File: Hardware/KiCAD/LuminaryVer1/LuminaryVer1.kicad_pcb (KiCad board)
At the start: 2 copper layers, 31 parts, among them J1 SPI_1_Connections, J10 ExtBattPwr, J2 SPI_2_Connections, J3 CAN_Connections, J4 ADC_Connections, J5 I2C_1_Connections, J6 I2C_2_Connections, J7 RS232_1_Connections, J8 RS232_2_Connections, J9 RS232_3_Connections, U1 74HC14, U2 STM32L432KBUx

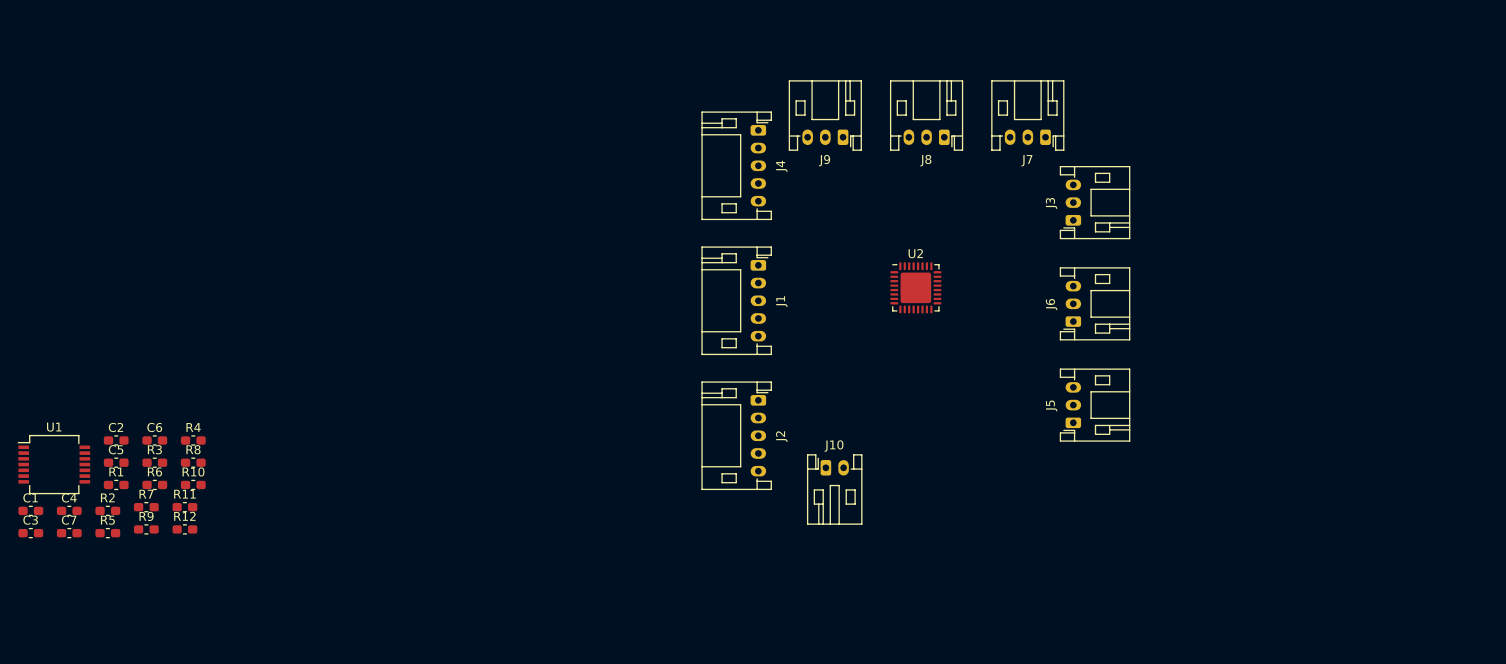
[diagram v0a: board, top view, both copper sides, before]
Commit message: Added PMIC and charging circuitry. Minor refresh of existing components. Added KiCAD component lib.
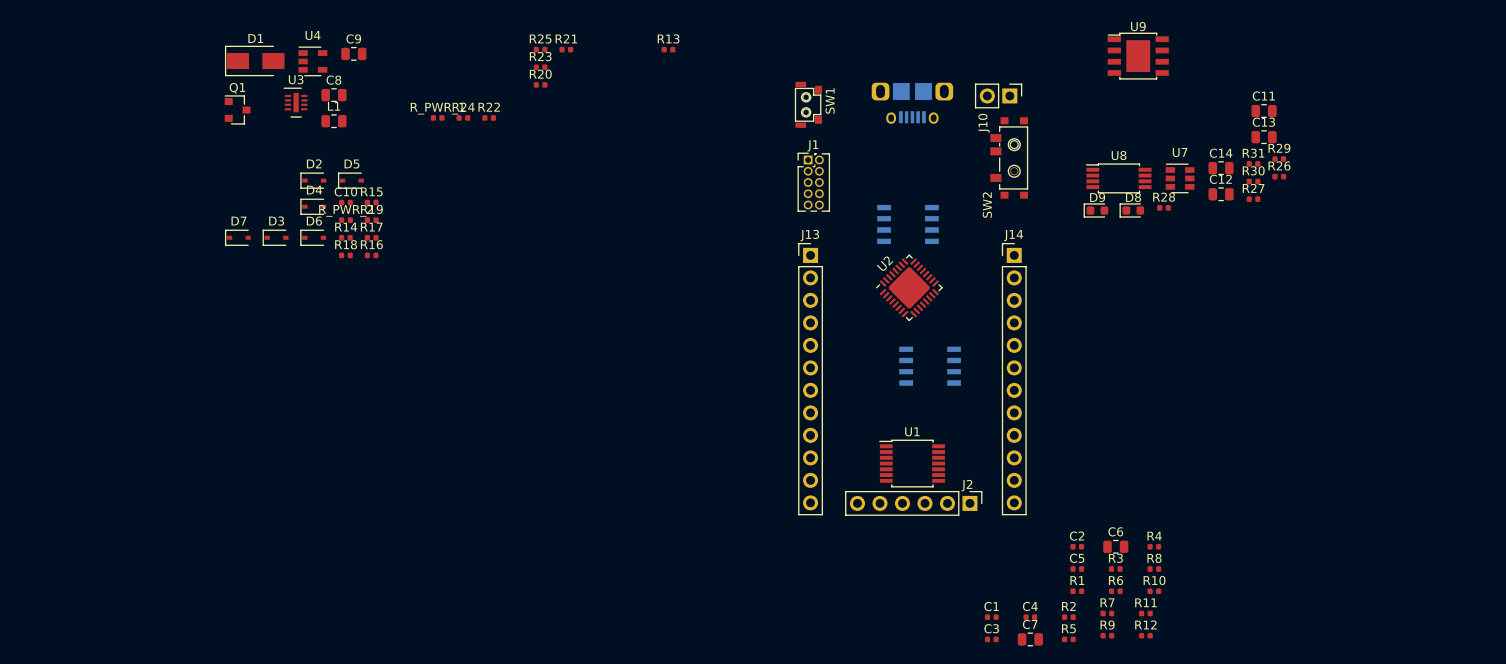
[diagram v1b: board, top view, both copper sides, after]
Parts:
- removed J3: CAN_Connections, Connector_JST:JST_PH_S3B-PH-K_1x03_P2.00mm_Horizontal
- removed J4: ADC_Connections, Connector_JST:JST_PH_S5B-PH-K_1x05_P2.00mm_Horizontal
- removed J5: I2C_1_Connections, Connector_JST:JST_PH_S3B-PH-K_1x03_P2.00mm_Horizontal
- removed J6: I2C_2_Connections, Connector_JST:JST_PH_S3B-PH-K_1x03_P2.00mm_Horizontal
- removed J7: RS232_1_Connections, Connector_JST:JST_PH_S3B-PH-K_1x03_P2.00mm_Horizontal
- removed J8: RS232_2_Connections, Connector_JST:JST_PH_S3B-PH-K_1x03_P2.00mm_Horizontal
- removed J9: RS232_3_Connections, Connector_JST:JST_PH_S3B-PH-K_1x03_P2.00mm_Horizontal
- added C10: 100nF, Capacitor_SMD:C_0402_1005Metric, F.Cu at (160.4, 64.0)
- added C11: 100nF, Capacitor_SMD:C_0805_2012Metric, F.Cu at (264.1, 53.7)
- added C12: 1uF, Capacitor_SMD:C_0805_2012Metric, F.Cu at (259.2, 63.1)
- added C13: 100nF, Capacitor_SMD:C_0805_2012Metric, F.Cu at (264.1, 56.6)
- added C14: 10uF, Capacitor_SMD:C_0805_2012Metric, F.Cu at (259.2, 60.1)
- added C8: 1uF, Capacitor_SMD:C_0805_2012Metric, F.Cu at (159.1, 51.9)
- added C9: 1uF, Capacitor_SMD:C_0805_2012Metric, F.Cu at (161.3, 47.2)
- added D1: SS16HE, Diode_SMD:D_SMA, F.Cu at (150.3, 48.0)
- added D2: 3v3Zener, Diode_SMD:D_SOD-323, F.Cu at (156.9, 61.6)
- added D3: 3v3Zener, Diode_SMD:D_SOD-323, F.Cu at (152.6, 68.0)
- added D4: 3v3Zener, Diode_SMD:D_SOD-323, F.Cu at (156.9, 64.5)
- added D5: 3v3Zener, Diode_SMD:D_SOD-323, F.Cu at (161.1, 61.6)
- added D6: 3v3Zener, Diode_SMD:D_SOD-323, F.Cu at (156.9, 68.0)
- added D7: 3v3Zener, Diode_SMD:D_SOD-323, F.Cu at (148.4, 68.0)
- added D8: RLED, Diode_SMD:D_0603_1608Metric, F.Cu at (249.3, 64.9)
- added D9: BLED, Diode_SMD:D_0603_1608Metric, F.Cu at (245.3, 64.9)
- added J12: USB_B_Micro, USB:Amphenol-MicroB, B.Cu at (224.4, 51.5)
- added J13: CN1, Connector_PinHeader_2.54mm:PinHeader_1x12_P2.54mm_Vertical, F.Cu at (212.9, 70.0)
- added J14: CN2, Connector_PinHeader_2.54mm:PinHeader_1x12_P2.54mm_Vertical, F.Cu at (235.9, 70.0)
- added L1: 4.3uH, Inductor_SMD:L_0805_2012Metric, F.Cu at (159.1, 54.9)
- added Q1: 2N3904, Package_TO_SOT_SMD:SOT-23, F.Cu at (148.2, 53.6)
- added R13: 0, Resistor_SMD:R_0402_1005Metric, F.Cu at (196.9, 46.8)
- added R14: 1.8k, Resistor_SMD:R_0402_1005Metric, F.Cu at (160.4, 68.0)
- added R15: 1.8k, Resistor_SMD:R_0402_1005Metric, F.Cu at (163.4, 64.0)
- added R16: 1.8k, Resistor_SMD:R_0402_1005Metric, F.Cu at (163.3, 70.0)
- added R17: 1.8k, Resistor_SMD:R_0402_1005Metric, F.Cu at (163.3, 68.0)
- added R18: 1.8k, Resistor_SMD:R_0402_1005Metric, F.Cu at (160.4, 70.0)
- added R19: 1.8k, Resistor_SMD:R_0402_1005Metric, F.Cu at (163.4, 66.0)
- added R20: 50k, Resistor_SMD:R_0402_1005Metric, F.Cu at (182.4, 50.8)
- added R21: 50k, Resistor_SMD:R_0402_1005Metric, F.Cu at (185.3, 46.8)
- added R22: 50k, Resistor_SMD:R_0402_1005Metric, F.Cu at (176.6, 54.5)
- added R23: 50k, Resistor_SMD:R_0402_1005Metric, F.Cu at (182.4, 48.8)
- added R24: 50k, Resistor_SMD:R_0402_1005Metric, F.Cu at (173.7, 54.5)
- added R25: 50k, Resistor_SMD:R_0402_1005Metric, F.Cu at (182.4, 46.8)
- added R26: 1k, Resistor_SMD:R_0402_1005Metric, F.Cu at (265.8, 61.1)
- added R27: 1k, Resistor_SMD:R_0402_1005Metric, F.Cu at (262.9, 63.6)
- added R28: 1k, Resistor_SMD:R_0402_1005Metric, F.Cu at (252.8, 64.6)
- added R29: 10k, Resistor_SMD:R_0402_1005Metric, F.Cu at (265.8, 59.1)
- added R30: 100, Resistor_SMD:R_0402_1005Metric, F.Cu at (262.9, 61.7)
- added R31: 50k, Resistor_SMD:R_0402_1005Metric, F.Cu at (262.9, 59.7)
- added R_PWR_1: 0, Resistor_SMD:R_0402_1005Metric, F.Cu at (170.8, 54.5)
- added R_PWR_2: 0, Resistor_SMD:R_0402_1005Metric, F.Cu at (160.4, 66.0)
- added SW1: SW_Push, button:LCSC_C255808_HYP_2x4x3.5mm_RightAngle, F.Cu at (212.4, 53.0)
- added SW2: SW_BATT_DISCONNECT, toggle:LCSC_C136659_HRO_SPDT_6.7x2.6mm_ToggleSwitch, F.Cu at (235.9, 59.0)
- added U3: DIO6605, Package_DFN_QFN:DFN-8-1EP_2x3mm_P0.5mm_EP0.61x2.2mm, F.Cu at (154.8, 52.8)
- added U4: AP2112K-3.3, Package_TO_SOT_SMD:SOT-23-5, F.Cu at (156.7, 48.1)
- added U5: SN65HVD232, Package_SO:SOIC-8_3.9x4.9mm_P1.27mm, B.Cu at (226.4, 82.5)
- added U6: AT25SF081-SSHD-X, Package_SO:SOIC-8_3.9x4.9mm_P1.27mm, B.Cu at (223.9, 66.5)
- added U7: DW01, Package_TO_SOT_SMD:SOT-23-6, F.Cu at (254.6, 61.3)
- added U8: FS8205A, Package_SO:TSSOP-8_4.4x3mm_P0.65mm, F.Cu at (247.7, 61.3)
- added U9: TP4056, PMIC:TP4056_SOP-8-PP, F.Cu at (249.9, 47.5)
- C1, C2, C3, C4, C5: footprint Capacitor_SMD:C_0603_1608Metric_Pad1.05x0.95mm_HandSolder -> Capacitor_SMD:C_0402_1005Metric
- C6, C7: value 100nF -> 10uF; footprint Capacitor_SMD:C_0603_1608Metric_Pad1.05x0.95mm_HandSolder -> Capacitor_SMD:C_0805_2012Metric
- J1: value SPI_1_Connections -> JTAG; footprint Connector_JST:JST_PH_S5B-PH-K_1x05_P2.00mm_Horizontal -> Connector_PinHeader_1.27mm:PinHeader_2x05_P1.27mm_Vertical
- J10: footprint Connector_JST:JST_PH_S2B-PH-K_1x02_P2.00mm_Horizontal -> Connector_PinHeader_2.54mm:PinHeader_1x02_P2.54mm_Vertical
- J2: value SPI_2_Connections -> GPIOInput; footprint Connector_JST:JST_PH_S5B-PH-K_1x05_P2.00mm_Horizontal -> Connector_PinHeader_2.54mm:PinHeader_1x06_P2.54mm_Vertical
- R1, R10, R2, R4, R5, R6, R7: value 10k -> 50k; footprint Resistor_SMD:R_0603_1608Metric_Pad1.05x0.95mm_HandSolder -> Resistor_SMD:R_0402_1005Metric
- R11, R3, R9: footprint Resistor_SMD:R_0603_1608Metric_Pad1.05x0.95mm_HandSolder -> Resistor_SMD:R_0402_1005Metric
- R12: value 10k -> 120; footprint Resistor_SMD:R_0603_1608Metric_Pad1.05x0.95mm_HandSolder -> Resistor_SMD:R_0402_1005Metric
- R8: value 10k -> 100; footprint Resistor_SMD:R_0603_1608Metric_Pad1.05x0.95mm_HandSolder -> Resistor_SMD:R_0402_1005Metric
- U1: footprint Package_SO:SSOP-14_5.3x6.2mm_P0.65mm -> Package_SO:TSSOP-14_4.4x5mm_P0.65mm
- moved C1 109.2 mm to (233.4, 110.8)
- moved C2 109.2 mm to (243.0, 102.9)
- moved C3 109.2 mm to (233.4, 113.4)
- moved C4 109.2 mm to (237.7, 110.8)
- moved C5 109.2 mm to (243.0, 105.4)
- moved C6 109.2 mm to (247.4, 102.9)
- moved C7 109.2 mm to (237.7, 113.4)
- moved R1 109.2 mm to (243.0, 107.9)
- moved R10 109.2 mm to (251.7, 107.9)
- moved R11 109.2 mm to (250.8, 110.4)
- moved R12 109.2 mm to (250.8, 112.9)
- moved R2 109.2 mm to (242.1, 110.8)
- moved R3 109.2 mm to (247.4, 105.4)
- moved R4 109.2 mm to (251.7, 102.9)
- moved R5 109.2 mm to (242.1, 113.4)
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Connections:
- net Net-(U2-Pad10) renamed /Processor/ADC_2
- net Net-(U2-Pad29) renamed /Output Connectors/I2C_1_SCL
- net Net-(U2-Pad6) renamed /Processor/ADC_0
- net Net-(U2-Pad9) renamed /Processor/ADC_1
- C1 pad 1: Net-(C1-Pad1) -> GND
- C1 pad 2: GND -> /Input Connectors/nRESET
- C2 pad 1: Net-(C2-Pad1) -> GND
- C2 pad 2: GND -> Net-(C2-Pad2)
- C3 pad 1: Net-(C3-Pad1) -> +3V3
- C4 pad 1: Net-(C4-Pad1) -> GND
- C4 pad 2: GND -> +3V3
- C5 pad 1: Net-(C5-Pad1) -> GND
- C5 pad 2: GND -> Net-(C5-Pad2)
- C6 pad 1: Net-(C6-Pad1) -> GND
- C6 pad 2: GND -> Net-(C6-Pad2)
- C7 pad 1: GND -> +5V
- C7 pad 2: +3V3 -> GND
- J1 pad 1: /Output Connectors/SPI_1_SCK -> +3V3
- J1 pad 2: /Output Connectors/SPI_1_MOSI -> /Processor/SWDIO
- J1 pad 3: /Output Connectors/SPI_1_MISO -> GND
- J1 pad 4: /Output Connectors/SPI_1_CS -> /Processor/SWCLK
- J1 pad 5: /Output Connectors/SPI_1_GND -> GND
- J2 pad 1: /Output Connectors/SPI_2_SCK -> Net-(J2-Pad1)
- J2 pad 2: /Output Connectors/SPI_2_MOSI -> Net-(J2-Pad2)
- J2 pad 3: /Output Connectors/SPI_2_MISO -> Net-(J2-Pad3)
- J2 pad 4: /Output Connectors/SPI_2_CS -> Net-(J2-Pad4)
- J2 pad 5: /Output Connectors/SPI_2_GND -> Net-(J2-Pad5)
- R1 pad 1: Net-(R1-Pad1) -> /Input Connectors/GPIO_INPUT_0
- R1 pad 2: +3V3 -> /Processor/GPIO_0
- R10 pad 1: Net-(C4-Pad1) -> +5V
- R10 pad 2: Net-(R10-Pad2) -> Net-(Q1-Pad3)
- R11 pad 1: Net-(C5-Pad1) -> /Input Connectors/nRESET
- R11 pad 2: Net-(R11-Pad2) -> +3V3
- R12 pad 1: Net-(C6-Pad1) -> /Output Connectors/CAN_1_HI
- R12 pad 2: Net-(R12-Pad2) -> /Output Connectors/CAN_1_LO
- R2 pad 1: Net-(R2-Pad1) -> /Processor/GPIO_1
- R2 pad 2: +3V3 -> /Input Connectors/GPIO_INPUT_1
- R3 pad 2: +3V3 -> GND
- R4 pad 1: Net-(C1-Pad1) -> /Output Drive/GPIO_IN_4
- R4 pad 2: Net-(R1-Pad1) -> /Input Connectors/GPIO_INPUT_4
- R5 pad 1: Net-(C2-Pad1) -> /Output Drive/GPIO_IN_5
- R5 pad 2: Net-(R2-Pad1) -> /Input Connectors/GPIO_INPUT_5
- R6 pad 1: Net-(C3-Pad1) -> /Processor/GPIO_2
- R6 pad 2: Net-(R3-Pad1) -> /Input Connectors/GPIO_INPUT_2
- R7 pad 1: Net-(R10-Pad2) -> /Output Drive/GPIO_IN_3
- R7 pad 2: +3V3 -> /Input Connectors/GPIO_INPUT_3
- R8 pad 1: Net-(R11-Pad2) -> Net-(Q1-Pad2)
- R8 pad 2: +3V3 -> /Power Supply/Ext_In+
- R9 pad 1: Net-(R12-Pad2) -> GND
- R9 pad 2: +3V3 -> Net-(Q1-Pad2)
- U1 pad 1: Net-(C1-Pad1) -> Net-(J2-Pad1)
- U1 pad 10: /GPIO Inputs/GPIO_USER_PIN_1 -> /Input Connectors/GPIO_INPUT_4
- U1 pad 11: Net-(C5-Pad1) -> Net-(J2-Pad5)
- U1 pad 12: /GPIO Inputs/GPIO_USER_PIN_2 -> /Input Connectors/GPIO_INPUT_5
- U1 pad 13: Net-(C6-Pad1) -> Net-(J2-Pad6)
- U1 pad 14: +3V3 -> Net-(C5-Pad2)
- U1 pad 2: /GPIO Inputs/GPIO_PWR_TOGGLE -> /Input Connectors/GPIO_INPUT_0
- U1 pad 3: Net-(C2-Pad1) -> Net-(J2-Pad2)
- U1 pad 4: /GPIO Inputs/GPIO_BRIGHTNESS_UP -> /Input Connectors/GPIO_INPUT_1
- U1 pad 5: Net-(C3-Pad1) -> Net-(J2-Pad3)
- U1 pad 6: /GPIO Inputs/GPIO_BRIGHTNESS_DN -> /Input Connectors/GPIO_INPUT_2
- U1 pad 8: /GPIO Inputs/GPIO_MODE_CHANGE -> /Input Connectors/GPIO_INPUT_3
- U1 pad 9: Net-(C4-Pad1) -> Net-(J2-Pad4)
- U2 pad 1: Net-(U2-Pad1) -> +3V3
- U2 pad 11: Net-(U2-Pad11) -> /Output Connectors/SPI_1_SCK
- U2 pad 12: Net-(U2-Pad12) -> /Output Connectors/SPI_1_MISO
- U2 pad 13: Net-(U2-Pad13) -> /Output Connectors/SPI_1_MOSI
- U2 pad 14: Net-(U2-Pad14) -> /Processor/GPIO_0
- U2 pad 15: Net-(U2-Pad15) -> /Processor/GPIO_1
- U2 pad 16: Net-(U2-Pad16) -> GND
- U2 pad 17: Net-(U2-Pad17) -> +3V3
- U2 pad 18: Net-(U2-Pad18) -> /Processor/GPIO_2
- U2 pad 19: Net-(U2-Pad19) -> /Output Connectors/RS232_1_TX
- U2 pad 20: Net-(U2-Pad20) -> /Output Connectors/RS232_1_RX
- U2 pad 21: Net-(U2-Pad21) -> /Processor/CAN_1_RX
- U2 pad 22: Net-(U2-Pad22) -> /Processor/CAN_1_TX
- U2 pad 23: Net-(U2-Pad23) -> /Processor/SWDIO
- U2 pad 24: Net-(U2-Pad24) -> /Processor/SWCLK
- U2 pad 25: Net-(U2-Pad25) -> /Output Drive/GPIO_IN_3
- U2 pad 26: Net-(U2-Pad26) -> /Output Connectors/SPI_2_SCK
- U2 pad 27: Net-(U2-Pad27) -> /Output Connectors/SPI_2_MISO
- U2 pad 28: Net-(U2-Pad28) -> /Output Connectors/SPI_2_MOSI
- U2 pad 3: Net-(U2-Pad3) -> FlashCS
- U2 pad 30: Net-(U2-Pad30) -> /Output Connectors/I2C_1_SDA
- U2 pad 31: Net-(U2-Pad31) -> Net-(R3-Pad1)
- U2 pad 32: Net-(U2-Pad32) -> GND
- U2 pad 33: Net-(U2-Pad33) -> GND
- U2 pad 4: Net-(U2-Pad4) -> /Input Connectors/nRESET
- U2 pad 5: Net-(U2-Pad5) -> +3V3
- U2 pad 7: Net-(U2-Pad7) -> /Output Drive/GPIO_IN_4
- U2 pad 8: Net-(U2-Pad8) -> /Output Drive/GPIO_IN_5

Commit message: Routed entire power section
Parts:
- removed C12, C8: 1uF, Capacitor_SMD:C_0805_2012Metric
- removed C14: 10uF, Capacitor_SMD:C_0805_2012Metric
- added D10: GLED, Diode_SMD:D_0603_1608Metric, F.Cu at (250.4, 73.5)
- added R32: 10k, Resistor_SMD:R_0402_1005Metric, F.Cu at (253.9, 73.2)
- J12: moved to F.Cu
- R30: value 100 -> 120
- moved C10 95.5 mm to (252.1, 90.8)
- moved R16 95.5 mm to (255.0, 96.8)
- moved R17 95.5 mm to (255.0, 94.8)
- moved R22 95.5 mm to (268.3, 81.3)
- moved R_PWR_1 95.5 mm to (262.5, 81.3)
- moved R_PWR_2 95.5 mm to (252.1, 92.8)
- moved D2 95.5 mm to (248.6, 88.4)
- moved D3 95.5 mm to (244.3, 94.8)
- moved D4 95.5 mm to (248.6, 91.3)
- moved D5 95.5 mm to (252.8, 88.4)
- moved D6 95.5 mm to (248.6, 94.8)
- moved D7 95.5 mm to (240.1, 94.8)
- moved R14 95.5 mm to (252.1, 94.8)
- moved R15 95.5 mm to (255.1, 90.8)
- moved R18 95.5 mm to (252.1, 96.8)
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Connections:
- U2 pad 2: Net-(U2-Pad2) -> StatusLED
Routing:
- net GND: track 0.00 -> 59.6 mm, vias 0 -> 9
- net /Power Supply/Ext_In+: track 0.00 -> 28.2 mm
- net /Input Connectors/nRESET: track 0.00 -> 25.4 mm, vias 0 -> 1
- net /Input Connectors/Batt_V+: track 0.00 -> 20.1 mm
- net Net-(R27-Pad1): track 0.00 -> 15.1 mm, vias 0 -> 2
- net Net-(R28-Pad1): track 0.00 -> 15.0 mm, vias 0 -> 2
- net /Input Connectors/Batt_V-: track 0.00 -> 12.8 mm
- net Net-(Q1-Pad3): track 0.00 -> 11.5 mm, vias 0 -> 2
- net +5V: track 0.00 -> 8.23 mm
- net Net-(C6-Pad2): track 0.00 -> 7.05 mm
- net Net-(U7-Pad1): track 0.00 -> 6.01 mm
- net Net-(C13-Pad1): track 0.00 -> 4.96 mm
- net Net-(U7-Pad3): track 0.00 -> 4.72 mm
- net Net-(R26-Pad1): track 0.00 -> 3.80 mm
- net Net-(Q1-Pad2): track 0.00 -> 2.38 mm
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- added copper zone on F.Cu, net +5V
- added copper zone on F.Cu, net GND
- added copper zone on In2.Cu, net GND
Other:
- copper layers 2 -> 4
- net class Signal added: clearance 0.2, trace_width 0.381, via_dia 0.45, via_drill 0.2
- rule via_min_drill: 0.3 -> 0.2
- rule via_min_size: 0.4 -> 0.45
- board text added: "CHRG"
- board text added: "STBY"

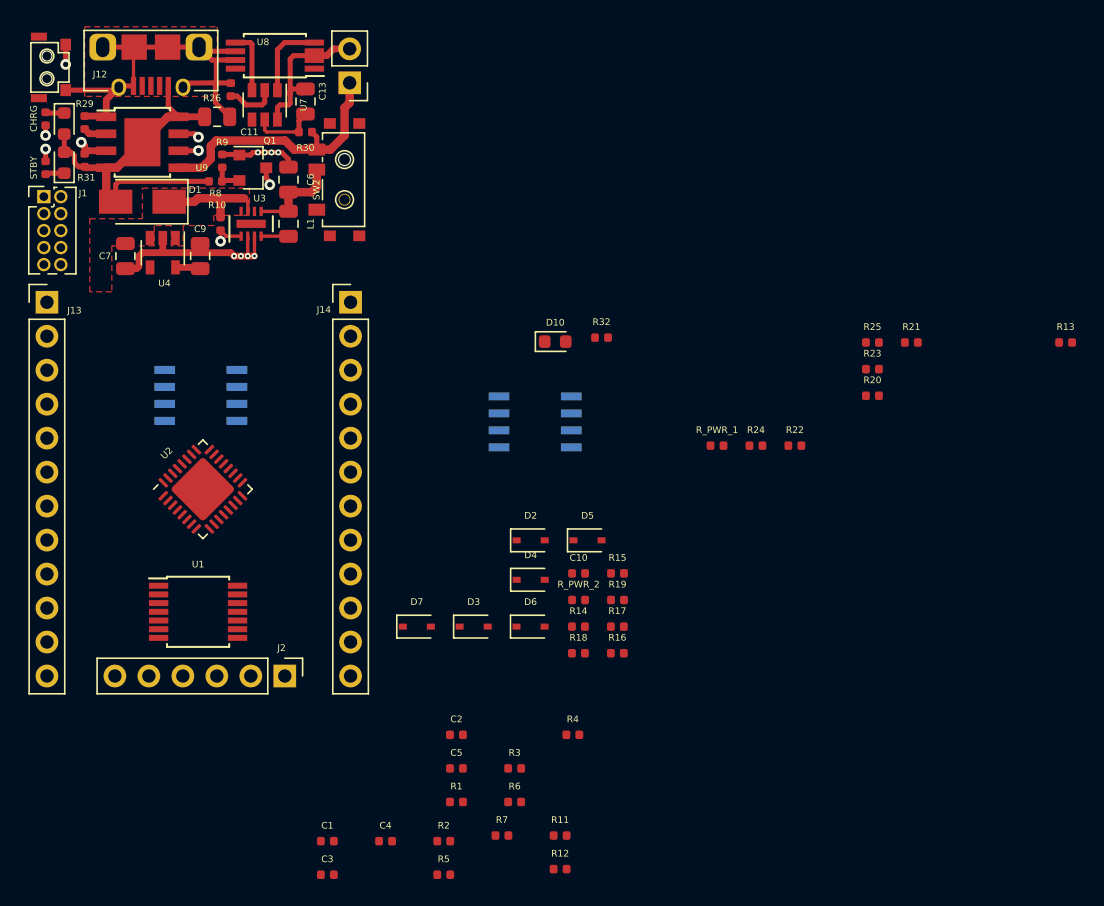
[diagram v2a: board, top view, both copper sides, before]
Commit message: Added majority of the logic level circuitry. Almost done routing connections.
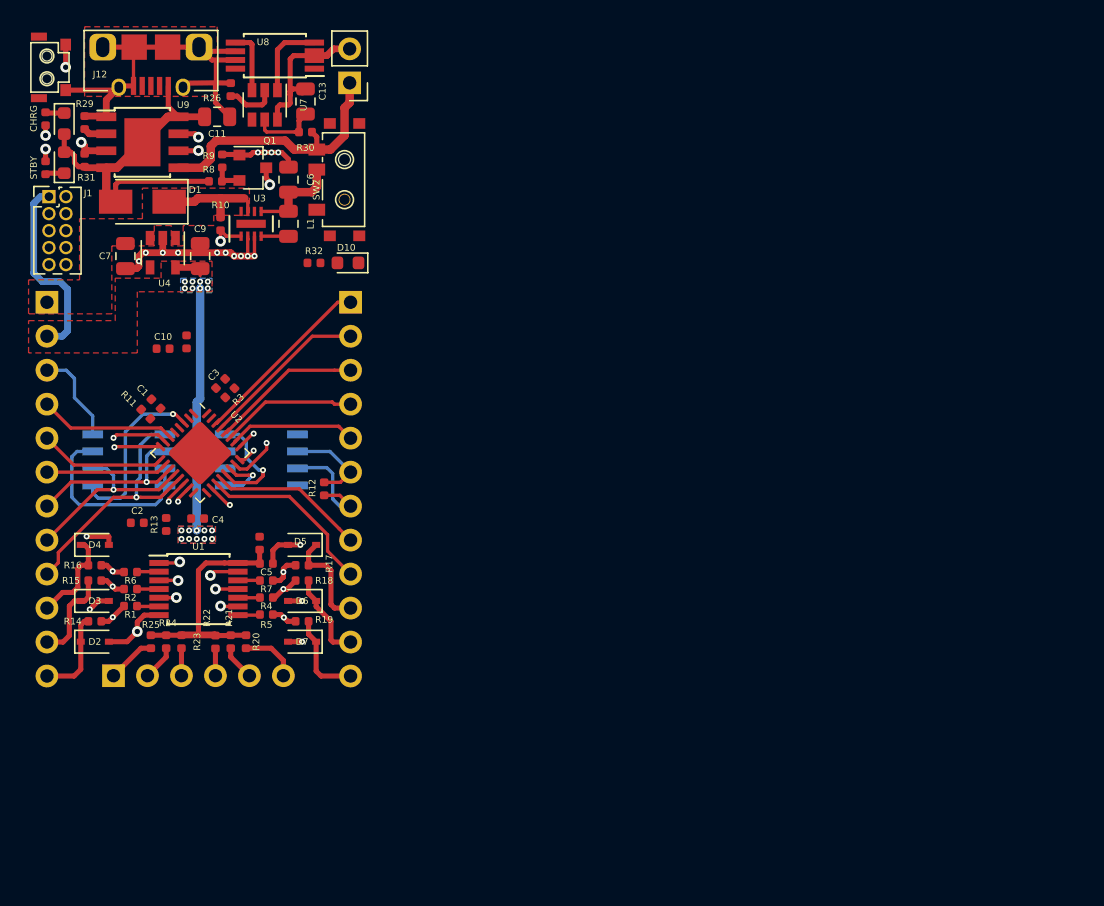
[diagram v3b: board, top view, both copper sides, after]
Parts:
- J13, J14, J2: moved to B.Cu
- moved R13 68.6 mm to (221.3, 87.2), turned to 270 degrees
- moved R25 58.4 mm to (220.2, 95.9), turned to 270 degrees
- moved R21 55.6 mm to (226.1, 95.9), turned to 270 degrees
- moved R23 55.5 mm to (222.5, 95.9), turned to 270 degrees
- moved R20 50.3 mm to (227.3, 95.9), turned to 270 degrees
- moved R24 46.5 mm to (221.3, 95.9), turned to 270 degrees
- moved R22 45.7 mm to (225.0, 96.0), turned to 270 degrees
- moved R11 44.2 mm to (219.8, 78.9), turned to 135 degrees
- moved R16 39.6 mm to (216.0, 90.2)
- moved R15 39.1 mm to (216.0, 91.4)
- moved C3 37.6 mm to (225.4, 76.6), turned to 45 degrees
- moved R14 36.2 mm to (216.0, 94.4)
- moved C10 35.3 mm to (221.1, 74.0), turned to 180 degrees
- moved R3 35.2 mm to (226.1, 77.3), turned to 45 degrees
- moved C1 35.1 mm to (220.6, 78.2), turned to 315 degrees
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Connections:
- net /Output Drive/GPIO_IN_3 renamed /Processor/GPIO_3
- J13 pad 1: Net-(J13-Pad1) -> +5V
- J13 pad 10: Net-(J13-Pad10) -> /Output Connectors/GPIO_OUT_2
- J13 pad 11: Net-(J13-Pad11) -> /Output Connectors/GPIO_OUT_1
- J13 pad 12: Net-(J13-Pad12) -> /Output Connectors/GPIO_OUT_0
- J13 pad 2: Net-(J13-Pad2) -> +3V3
- J13 pad 3: Net-(J13-Pad3) -> GND
- J13 pad 4: Net-(J13-Pad4) -> /Processor/ADC_0
- J13 pad 5: Net-(J13-Pad5) -> /Processor/ADC_1
- J13 pad 6: Net-(J13-Pad6) -> /Processor/ADC_2
- J13 pad 7: Net-(J13-Pad7) -> /Output Connectors/SPI_1_SCK
- J13 pad 8: Net-(J13-Pad8) -> /Output Connectors/SPI_1_MISO
- J13 pad 9: Net-(J13-Pad9) -> /Output Connectors/SPI_1_MOSI
- J14 pad 1: Net-(J14-Pad1) -> /Output Connectors/I2C_1_SDA
- J14 pad 10: Net-(J14-Pad10) -> /Output Connectors/GPIO_OUT_3
- J14 pad 11: Net-(J14-Pad11) -> /Output Connectors/GPIO_OUT_4
- J14 pad 12: Net-(J14-Pad12) -> /Output Connectors/GPIO_OUT_5
- J14 pad 2: Net-(J14-Pad2) -> /Output Connectors/I2C_1_SCL
- J14 pad 3: Net-(J14-Pad3) -> /Output Connectors/SPI_2_MOSI
- J14 pad 4: Net-(J14-Pad4) -> /Output Connectors/SPI_2_MISO
- J14 pad 5: Net-(J14-Pad5) -> /Output Connectors/SPI_2_SCK
- J14 pad 6: Net-(J14-Pad6) -> /Output Connectors/CAN_1_LO
- J14 pad 7: Net-(J14-Pad7) -> /Output Connectors/CAN_1_HI
- J14 pad 8: Net-(J14-Pad8) -> /Output Connectors/RS232_1_RX
- J14 pad 9: Net-(J14-Pad9) -> /Output Connectors/RS232_1_TX
- R18 pad 2: /Output Drive/GPIO_IN_4 -> /Processor/GPIO_4
- R19 pad 2: /Output Drive/GPIO_IN_5 -> /Processor/GPIO_5
- R4 pad 1: /Output Drive/GPIO_IN_4 -> /Processor/GPIO_4
- R5 pad 1: /Output Drive/GPIO_IN_5 -> /Processor/GPIO_5
- U1 pad 1: Net-(J2-Pad1) -> Net-(J2-Pad3)
- U1 pad 12: /Input Connectors/GPIO_INPUT_5 -> /Input Connectors/GPIO_INPUT_3
- U1 pad 13: Net-(J2-Pad6) -> Net-(J2-Pad4)
- U1 pad 2: /Input Connectors/GPIO_INPUT_0 -> /Input Connectors/GPIO_INPUT_2
- U1 pad 5: Net-(J2-Pad3) -> Net-(J2-Pad1)
- U1 pad 6: /Input Connectors/GPIO_INPUT_2 -> /Input Connectors/GPIO_INPUT_0
- U1 pad 8: /Input Connectors/GPIO_INPUT_3 -> /Input Connectors/GPIO_INPUT_5
- U1 pad 9: Net-(J2-Pad4) -> Net-(J2-Pad6)
- U2 pad 14: /Processor/GPIO_0 -> /Processor/GPIO_2
- U2 pad 15: /Processor/GPIO_1 -> /Processor/GPIO_5
- U2 pad 18: /Processor/GPIO_2 -> /Processor/GPIO_4
- U2 pad 7: /Output Drive/GPIO_IN_4 -> /Processor/GPIO_0
- U2 pad 8: /Output Drive/GPIO_IN_5 -> /Processor/GPIO_1
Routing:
- net +3V3: track 1.88 -> 35.0 mm, vias 0 -> 18
- net /Processor/SWDIO: track 0.00 -> 28.9 mm, vias 0 -> 1
- net /Processor/SWCLK: track 0.00 -> 25.0 mm, vias 0 -> 1
- net GND: track 59.6 -> 80.9 mm, vias 9 -> 21
- net /Processor/GPIO_0: track 0.00 -> 21.1 mm, vias 0 -> 2
- net /Output Connectors/SPI_1_MOSI: track 0.00 -> 19.5 mm, vias 0 -> 1
- net Net-(C5-Pad2): track 0.00 -> 17.9 mm
- net /Processor/GPIO_5: track 0.00 -> 17.0 mm, vias 0 -> 2
- net /Processor/GPIO_1: track 0.00 -> 16.5 mm, vias 0 -> 2
- net /Processor/GPIO_3: track 0.00 -> 16.0 mm, vias 0 -> 2
- net Net-(J2-Pad1): track 0.00 -> 14.7 mm, vias 0 -> 1
- net Net-(J2-Pad6): track 0.00 -> 14.6 mm, vias 0 -> 1
- net /Output Connectors/SPI_1_MISO: track 0.00 -> 14.4 mm, vias 0 -> 1
- net Net-(C2-Pad2): track 0.00 -> 14.2 mm
- net /Output Connectors/SPI_1_SCK: track 0.00 -> 13.8 mm, vias 0 -> 1
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- added copper zone on B.Cu, net +3V3
- added copper zone on F.Cu, net +3V3

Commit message: Finalized for version 1 production.
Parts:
- C10, C2, R_PWR_2: moved to B.Cu
- C11, C13: footprint Capacitor_SMD:C_0805_2012Metric -> Capacitor_SMD:C_0402_1005Metric
- D2, D3, D4, D5, D6, D7: value 3v3Zener -> 3.9V
- L1: value 4.3uH -> 3.3uH
- R1, R10, R2, R20, R21, R22, R23, R24, R25, R31, R4, R5, R6, R7: value 50k -> 47k
- R14, R15, R16, R17, R18, R19: value 1.8k -> 2.0k
- R_PWR_3: renamed from R13; moved to B.Cu
- moved D10 20.2 mm to (216.4, 75.6), turned to 0 degrees
- moved R32 18.1 mm to (217.2, 77.5), turned to 270 degrees
- moved R_PWR_2 14.8 mm to (226.1, 88.0), turned to 0 degrees
- moved C10 13.6 mm to (226.1, 86.7), turned to 0 degrees
- moved C2 2.07 mm to (221.2, 86.7), turned to 180 degrees
- moved C3 1.55 mm to (223.9, 76.9), turned to 0 degrees
- moved C1 1.39 mm to (221.6, 77.2)
- moved R11 1.30 mm to (220.7, 78.0)
- moved R_PWR_3 0.77 mm to (221.2, 87.9), turned to 180 degrees
- moved C11 0.76 mm to (224.4, 56.7)
- moved C13 0.38 mm to (231.3, 55.5)
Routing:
- net +3V3: track 35.0 -> 57.5 mm, vias 18 -> 19
- net GND: track 80.9 -> 100.7 mm, vias 21 -> 31
- net /Input Connectors/nRESET: track 22.5 -> 40.2 mm, vias 1 -> 2
- net Net-(C10-Pad2): track 0.00 -> 9.31 mm
- net StatusLED: track 0.00 -> 6.71 mm, vias 0 -> 2
- net Net-(C2-Pad2): track 14.2 -> 16.6 mm
- net Net-(R3-Pad1): track 0.00 -> 1.99 mm
- net Net-(D10-Pad2): track 0.00 -> 1.50 mm
- net /Input Connectors/Batt_V-: track 12.8 -> 12.0 mm
- net /Processor/SWCLK: track 25.0 -> 25.8 mm
- net /Processor/SWDIO: track 28.9 -> 29.5 mm
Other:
- board outline added: 25.7 x 50 mm
- rule pad_to_mask_clearance: 0.051 -> -0.051
- board text added: "+3.3V"
- board text added: "+5.0v"
- board text added: "GND"
- board text added: "Luminary Ver 1.0"
